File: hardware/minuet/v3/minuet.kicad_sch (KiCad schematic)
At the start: 41 parts, among them J101 B2P-VH-B, J102 B2B-XH-A, J103 PPPC062LFBN-RC, J104 B2B-XH-A, Q101 MMBT3904, U101 TSOP39238, U102 LMV331IDCK

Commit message: First draft of Minuet v3.
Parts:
- removed NT103: NetTie_2, Generic:NetTie-2_SMD_Pad0.4mm, symbol Device:NetTie_2
- added J5: B2B-XH-A, Connector_JST:JST_XH_B2B-XH-A_1x02_P2.50mm_Vertical, symbol Connector_Generic:Conn_01x02
- added NT3: NetTie_2, Generic:NetTie-2_SMD_Pad0.2mm, symbol Device:NetTie_2
- J4: renamed from J103; value PPPC062LFBN-RC -> PPPC082LFBN-RC; footprint Connector_PinSocket_2.54mm:PinSocket_2x06_P2.54mm_Vertical -> Connector_PinSocket_2.54mm:PinSocket_2x08_P2.54mm_Vertical; symbol Connector_Generic:Conn_02x06_Odd_Even -> Connector_Generic:Conn_02x08_Odd_Even; LCSC C20071205 -> (none); Label EXPANSION -> (none)
- JP1: renamed from JP101; value SolderJumper_3_Bridged12 -> SolderJumper_2_Bridged; footprint Jumper:SolderJumper-3_P1.3mm_Bridged12_RoundedPad1.0x1.5mm -> Jumper:SolderJumper-2_P1.3mm_Bridged_RoundedPad1.0x1.5mm; symbol Jumper:SolderJumper_3_Bridged12 -> Jumper:SolderJumper_2_Bridged; Label VOLUME -> (none)
- renumbered BZ101 to BZ1, C101 to C1, C102 to C2, C103 to C3, C104 to C4, C105 to C5, C106 to C6, C107 to C7, D101 to D1, F101 to F1, J101 to J1, J102 to J2, J104 to J3, L101 to L1, NT101 to NT1, NT102 to NT2, Q101 to Q1, R101 to R1, R110 to R10, R113 to R11, R111 to R12, R112 to R13, R114 to R14, R115 to R15, R116 to R16, R102 to R2, R103 to R3, R104 to R4, R105 to R5, R106 to R6, R107 to R7, R108 to R8, R109 to R9, TP101 to TP1, TP102 to TP2, U101 to U1, U102 to U2, VR101 to VR1
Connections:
- net +12V: now also J4.16 (Pin_16); no longer J4.12 (Pin_12)
- net +3.3V: now also J4.14 (Pin_14); no longer J4.10 (Pin_10)
- net GND: now also J4.13 (Pin_13), J4.15 (Pin_15), J5.1 (Pin_1); no longer J4.11 (Pin_11), J4.9 (Pin_9)
- net GPIO5: now also J4.6 (Pin_6)
- net SCL: now also J4.7 (Pin_7); no longer J4.6 (Pin_6)
- net SDA: now also J4.8 (Pin_8); no longer J4.5 (Pin_5)
- net UART_RXD: now also J4.9 (Pin_9); no longer J4.7 (Pin_7)
- net UART_TXD: now also J4.10 (Pin_10); no longer J4.8 (Pin_8)
- net XIO13: now also R8.2
- net XIO14: now also R1.2; no longer R8.2
- net XIO15: now also NT3.1; no longer R1.2
- net VIN: now reaches C3.1, C4.1, NT2.2, VR1.3 (VIN), VR1.5 (EN)
- new net GPIO6: J4.5 (Pin_5)
- new net LOCK: J4.12 (Pin_12), J5.2 (Pin_2), NT3.2
- no-connect marks 0 -> 1
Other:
- sheet cover renamed lid
- sheet fan ports: added WAKE; removed DIR, NSLEEP, PWM, TACH
- sheet lid: file cover.kicad_sch -> lid.kicad_sch
- note added: "Driven at 3.3 V for politeness (12 V would be louder) Can be disabled in software or by cutting the solder jumper"
- note added: "Header for accessories and factory programming - GPIO0, GPIO1, GPIO5, GPIO6 can be used for any purpose - UART_RXD and UART_TXD provide the serial port - SCL and SDA provide the I2C bus (QWIIC) - RESET and BOOT are wired in parallel with their corresponding buttons (active low) - LOCK engages the safety lock (active low) - 12 V supply is unregulated, 1 A current available - 3.3 V supply is regula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"
- note added: "SAFETY LOCK"
- note added: "While the input is tied to ground, stops the fan, closes the lid, and inhibits operation"
- note removed: "Driven at 3.3 V for politeness (12 V will be louder) Can be disabled in software or by cutting the solder jumper"
- note removed: "Header for accessories and factory programming - GPIO0 and GPIO1 are free to be used for any purpose - UART_RXD and UART_TXD provide the serial port - SCL and SDA provide the I2C bus (QWIIC) - RESET and BOOT are wired in parallel with their corresponding buttons (active when tied to ground) - 12 V supply is unregulated, 1 A current available - 3.3 V supply is regulated, 600 mA current available"
- moved on the sheet: R11, R15, R16

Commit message: Prepare for fabrication.
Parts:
- C2, C4, C6, C7: LCSC (none) -> C14663
- C3: LCSC (none) -> C45783
- C5: LCSC (none) -> C16780
- J4: LCSC (none) -> C2897409
- L1: LCSC C39846631 -> C22416628
- Q1: LCSC C239187 -> C20526; LCSC_Alternative (none) -> C239187
- R1, R11, R15, R16, R5, R6, R7, R8: LCSC (none) -> C25804
- R10, R12, R13, R2: LCSC (none) -> C25803
- R14: value 1.5M -> 1M; LCSC (none) -> C22935
- R3: LCSC (none) -> C21190
- R4: LCSC (none) -> C4216
- R9: value 100K -> 68K; LCSC (none) -> C23231
- VR1: FT Rotation Offset (none) -> 180
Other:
- note added: "Originally designed using 100 K / 1.5 M in the voltage divider for symmetry with the input impedance but 1.5 M is not considered a basic part at JLCPCB. Substituted other resistor values in a similar ratio."

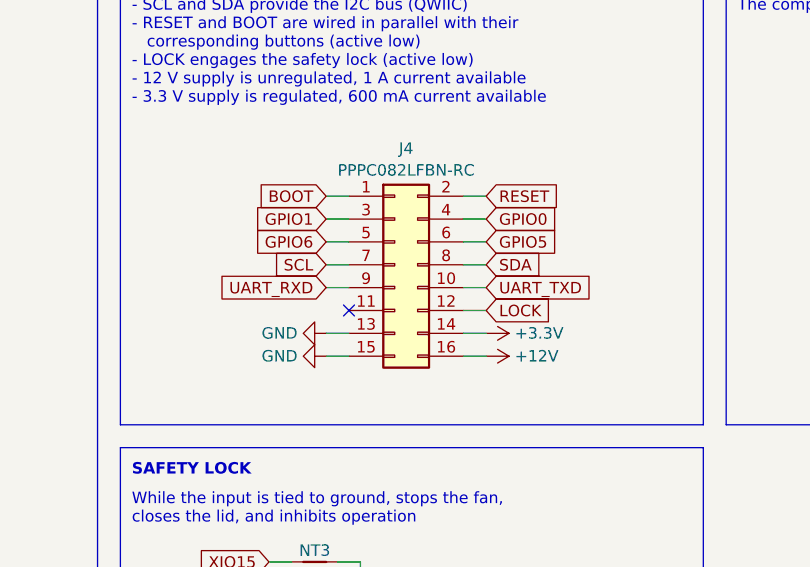
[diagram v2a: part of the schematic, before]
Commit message: Remove unnecessary fields.
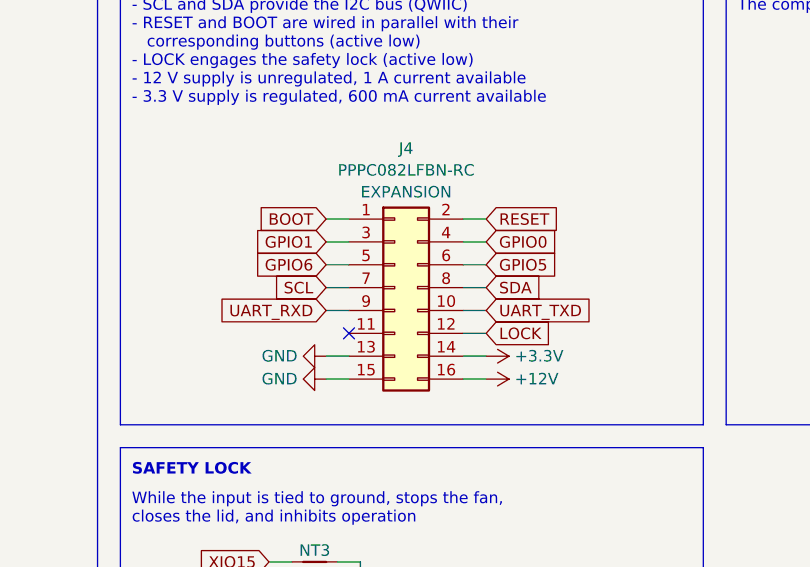
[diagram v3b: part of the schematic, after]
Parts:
- J4: Label (none) -> EXPANSION
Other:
- moved on the sheet: J4

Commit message: Prepare Minuet v3 for production.
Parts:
- C1: Alternative (none) -> A750KW687M1EAAE016; LCSC C1020064 -> C5243855; Part A750KW687M1EAAE016 -> (none)
- C2, C4: Rating 25V, X5R -> 50V, X5R
- C6, C7: Rating 6.3V, X5R -> 50V, X5R
- F1: LCSC C468987 -> C135392; LCSC_Alternative (none) -> C3646894, C135392; LCSC_Preferred (none) -> C1562203, C468987
- J2, J3, J5: FT Rotation Offset (none) -> 180
- renumbered R9 to R10, R12 to R11, R11 to R12, R10 to R9
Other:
- note added: "Input must be 9 to 16 V Circuit protection - Internal: 4 A polyfuse and TVS - External: 5 A fuse recommended"
- note removed: "Input must be 9 to 16 V Circuit protection - Internal: 4 A polyfuse and TVS - External: 5 A fuse"
- moved on the sheet: BZ1, C1, C7, D1, F1, J1, J2, J3, J5, JP1, NT3, Q1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
